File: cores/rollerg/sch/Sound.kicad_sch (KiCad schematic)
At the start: 0 parts

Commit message: wip rollerg sch: objects page
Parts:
- added C1: 053260, symbol konami:053260
- added CN2: Conn_02x32_Row_Letter_First, symbol Connector_Generic:Conn_02x32_Row_Letter_First
- added D1: 065A08, symbol konami:065A08
- added F1: 74LS04, symbol jt74:74LS04
- added JP1: JP_2_Bridged, symbol Jumper:Jumper_2_Bridged
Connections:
- new net: C1.28 (SO), JP1.1 (A)
- new net: C1.71 (S~{RD}), F1.4
- new net AUX1: C1.23 (AUX1)
- new net AUX2: C1.24 (AUX2), D1.13 (~{OE})
- new net MAIN_A1: C1.18 (MA0)
- new net MAIN_DB0: C1.8 (MDB0)
- new net MAIN_DB1: C1.9 (MDB1)
- new net MAIN_DB2: C1.10 (MDB2)
- new net MAIN_DB3: C1.11 (MDB3)
- new net MAIN_DB4: C1.13 (MDB4)
- new net MAIN_DB5: C1.14 (MDB5)
- new net MAIN_DB6: C1.15 (MDB6)
- new net MAIN_DB7: C1.16 (MDB7)
- new net MR/~{W}: C1.19 (~{MRW})
- new net PCMCLK: C1.21 (CLK)
- new net PCM~{CS}: C1.72 (~{CS})
- new net RA0: C1.39 (RA0), CN2.b6 (Pin_b6), D1.30 (D15/A-1)
- new net RA1: C1.40 (RA1), CN2.b7 (Pin_b7), D1.10 (A0)
- new net RA10: C1.50 (RA10), CN2.b20 (Pin_b20), D1.40 (A9)
- new net RA11: C1.51 (RA11), CN2.a16 (Pin_a16), D1.39 (A10)
- new net RA12: C1.53 (RA12), CN2.a6 (Pin_a6), D1.38 (A11)
- new net RA13: C1.54 (RA13), CN2.a7 (Pin_a7), D1.37 (A12)
- new net RA14: C1.55 (RA14), CN2.a8 (Pin_a8), D1.36 (A13)
- new net RA15: C1.56 (RA15), CN2.a9 (Pin_a9), D1.35 (A14)
- new net RA16: C1.57 (RA16), CN2.a10 (Pin_a10), D1.34 (A15)
- new net RA17: C1.58 (RA17), CN2.a11 (Pin_a11), D1.33 (A16)
- new net RA18: C1.59 (RA18), CN2.a13 (Pin_a13), D1.2 (A17)
- new net RA19: C1.60 (RA19), CN2.a14 (Pin_a14), D1.1 (A18)
- new net RA2: C1.41 (RA2), CN2.b8 (Pin_b8), D1.9 (A1)
- new net RA20: C1.62 (RA20), CN2.a15 (Pin_a15), D1.42 (A19)
- new net RA3: C1.42 (RA3), CN2.b9 (Pin_b9), D1.8 (A2)
- new net RA4: C1.44 (RA4), CN2.b10 (Pin_b10), D1.7 (A3)
- new net RA5: C1.45 (RA5), CN2.b11 (Pin_b11), D1.6 (A4)
- new net RA6: C1.46 (RA6), CN2.b12 (Pin_b12), D1.5 (A5)
- new net RA7: C1.47 (RA7), CN2.b13 (Pin_b13), D1.4 (A6)
- new net RA8: C1.48 (RA8), CN2.b14 (Pin_b14), D1.3 (A7)
- new net RA9: C1.49 (RA9), CN2.b15 (Pin_b15), D1.41 (A8)
- new net RD0: C1.29 (RD0), CN2.b24 (Pin_b24), D1.14 (D0)
- new net RD1: C1.30 (RD1), CN2.b25 (Pin_b25), D1.16 (D1)
- new net RD2: C1.31 (RD2), CN2.b26 (Pin_b26), D1.18 (D2)
- new net RD3: C1.32 (RD3), CN2.b27 (Pin_b27), D1.20 (D3)
- new net RD4: C1.35 (RD4), CN2.a27 (Pin_a27), D1.23 (D4)
- new net RD5: C1.36 (RD5), CN2.a26 (Pin_a26), D1.25 (D5)
- new net RD6: C1.37 (RD6), CN2.a25 (Pin_a25), D1.27 (D6)
- new net RD7: C1.38 (RD7), CN2.a24 (Pin_a24), D1.29 (D7)
- new net SH1: C1.26 (SH1)
- new net SH2: C1.27 (SH2)
- new net SND_A0: C1.70 (AB0)
- new net SND_A1: C1.69 (AB1)
- new net SND_A2: C1.68 (AB2)
- new net SND_A3: C1.67 (AB3)
- new net SND_A4: C1.66 (AB4)
- new net SND_A5: C1.65 (AB5)
- new net SND_D0: C1.5 (DB0)
- new net SND_D1: C1.4 (DB1)
- new net SND_D2: C1.3 (DB2)
- new net SND_D3: C1.2 (DB3)
- new net SND_D4: C1.1 (DB4)
- new net SND_D5: C1.80 (DB5)
- new net SND_D6: C1.79 (DB6)
- new net SND_D7: C1.78 (DB7)
- new net SO: JP1.2 (B)
- new net STBI: C1.22 (STBI)
- new net SY: C1.25 (SY)
- new net S~{RD}: F1.3
- new net VCC: C1.20 (VCC), C1.33 (VCC), C1.73 (VCC), CN2.a1 (Pin_a1), CN2.a12 (Pin_a12), CN2.a17 (Pin_a17), CN2.a18 (Pin_a18), CN2.a19 (Pin_a19), CN2.a2 (Pin_a2), CN2.a3 (Pin_a3), CN2.a4 (Pin_a4), CN2.a5 (Pin_a5), CN2.b1 (Pin_b1), CN2.b16 (Pin_b16), CN2.b17 (Pin_b17), CN2.b18 (Pin_b18), CN2.b19 (Pin_b19), CN2.b2 (Pin_b2), CN2.b3 (Pin_b3), CN2.b4 (Pin_b4), CN2.b5 (Pin_b5), D1.11 (~{CE}), D1.22 (VCC), D1.31 (VCC)
- new net VSS: C1.12 (VSS), C1.34 (VSS), C1.43 (VSS), C1.52 (VSS), C1.61 (VSS), C1.74 (VSS), CN2.a20 (Pin_a20), CN2.a21 (Pin_a21), CN2.a22 (Pin_a22), CN2.a23 (Pin_a23), CN2.a28 (Pin_a28), CN2.a29 (Pin_a29), CN2.a30 (Pin_a30), CN2.a31 (Pin_a31), CN2.a32 (Pin_a32), CN2.b21 (Pin_b21), CN2.b22 (Pin_b22), CN2.b23 (Pin_b23), CN2.b28 (Pin_b28), CN2.b29 (Pin_b29), CN2.b30 (Pin_b30), CN2.b31 (Pin_b31), CN2.b32 (Pin_b32), D1.12 (VSS), D1.32 (BYTE)
- new net ~{MCS}: C1.17 (~{MCS})
- new net ~{SYSRES}: C1.75 (RESET)
- no-connect marks 0 -> 13
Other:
- note added: "NOT POPULATED"

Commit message: wip rollerg sch: SOUND
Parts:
- removed CN2: Conn_02x32_Row_Letter_First, symbol Connector_Generic:Conn_02x32_Row_Letter_First
- removed D1: 065A08, symbol konami:065A08
- added 30P, C49, C61: C, symbol Device:C
- added A1: 23C4100, symbol jt_rom:23C4100
- added B10: YM3012, symbol yamaha:YM3012_ALT
- added B8: LM324, symbol Amplifier_Operational:LM324
- added D6: YM3812-3526, symbol yamaha:YM3812-3526
- added E11: 27256, Package_DIP:DIP-28_W15.24mm, symbol Memory_EPROM:27256
- added E13: MB9416, symbol arcade:HM6116P-3
- added E4: Z80CPU, symbol CPU:Z80CPU
- added F16: 74LS08, symbol 74xx:74LS08
- added F6: 74LS138, symbol 74xx:74LS138
- added unit 4 of F7
- added G14: 74LS74, symbol jt74:74LS74
- added J1: XTAL_OSC, symbol Device:Crystal_GND23_Small
- added R15: 2.2K, symbol Device:R_US
- added R4: 560, symbol Device:R_US
- added YM1: YM3014, Package_SO:MSOP-12-1EP_3x4.039mm_P0.65mm_EP1.651x2.845mm, symbol yamaha:YM3014
- renumbered F1 to F7
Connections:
- net PCMCLK: now also D6.24 (øM), F7.8
- net PCM~{CS}: now also F6.10 (O5)
- net RA0: now also A1.29 ( D15 /A-1)
- net RA1: now also A1.9 (A0)
- net RA10: now also A1.39 (A9)
- net RA11: now also A1.38 (A10)
- net RA12: now also A1.37 (A11)
- net RA13: now also A1.36 (A12)
- net RA14: now also A1.35 (A13)
- net RA15: now also A1.34 (A14)
- net RA16: now also A1.33 (A15)
- net RA17: now also A1.32 (A16)
- net RA18: now also A1.1 (A17)
- net RA2: now also A1.8 (A1)
- net RA3: now also A1.7 (A2)
- net RA4: now also A1.6 (A3)
- net RA5: now also A1.5 (A4)
- net RA6: now also A1.4 (A5)
- net RA7: now also A1.3 (A6)
- net RA8: now also A1.2 (A7)
- net RA9: now also A1.40 (A8)
- net RD0: now also A1.13 (D0)
- net RD1: now also A1.15 (D1)
- net RD2: now also A1.17 (D2)
- net RD3: now also A1.19 (D3)
- net RD4: now also A1.22 (D4)
- net RD5: now also A1.24 (D5)
- net RD6: now also A1.26 (D6)
- net RD7: now also A1.28 (D7)
- net SH1: now also B10.6 (SAM1), G14.3 (C)
- net SH2: now also B10.5 (SAM2)
- net SND_A0: now also D6.4 (A0), E11.10 (A0), E13.19 (A10), E4.30 (A0)
- net SND_A1: now also E11.9 (A1), E13.8 (A0), E4.31 (A1)
- net SND_A2: now also E11.8 (A2), E13.4 (A4), E4.32 (A2)
- net SND_A3: now also E11.7 (A3), E13.7 (A1), E4.33 (A3)
- net SND_A4: now also E11.6 (A4), E13.6 (A2), E4.34 (A4)
- net SND_A5: now also E11.5 (A5), E13.5 (A3), E4.35 (A5)
- net SO: now also B10.4 (SD)
- net SY: now also B10.2 (ø1)
- net VCC: now also A1.21 (VCC), B10.1 (VCC), D6.1 (VCC), E11.1 (VPP), E11.28 (VCC), E13.24 (VCC), E4.11 (VCC), G14.10 (~{S}), G14.12 (D), J1.3, YM1.1 (VCC)
- net VSS: now also A1.10 (~{CE}), A1.11 (VSS), A1.12 (~{OE}), A1.30 (VSS), A1.31 (~{BYTE}), B10.16 (AVSS), B10.3 (DVSS), B10.8 (AVSS), C49.2, C61.2, D6.12 (VSS), E11.14 (GND), E13.12 (VSS), E4.29 (GND), F6.5 (E2), F6.8 (GND), G14.2 (D), J1.1, J1.2, R15.2, YM1.6 (VSS)
- net MAIN_DB0 renamed DB0
- net MAIN_DB1 renamed DB1
- net MAIN_DB2 renamed DB2
- net MAIN_DB3 renamed DB3
- net MAIN_DB4 renamed DB4
- net MAIN_DB5 renamed DB5
- net MAIN_DB6 renamed DB6
- net MAIN_DB7 renamed DB7
- net MR/~{W} renamed R/~{W}
- net ~{SYSRES} renamed RES
- net RES: now also B10.7 (~{ICL}), D6.3 (~{IC}), E4.26 (~{RESET}), F16.12, G14.1 (~{R})
- new net: 30P.1, B10.13 (MP), B8.1, R15.1
- new net: 30P.2, B10.14 (BC), B8.2 (-)
- new net: B10.12 (BUFF), B8.5 (+)
- new net: B8.6 (-), B8.7, R4.2
- new net: B10.9 (CH1), C49.1
- new net: F16.11, G14.13 (~{R})
- new net: B10.10 (CH2), C61.1
- new net: B10.11 (COM), R4.1
- new net: B10.15 (RB), B8.3 (+)
- new net: D6.5 (~{WR}), E13.21 (~{WR}), E4.22 (~{WR})
- new net: D6.7 (~{CS}), F6.9 (O6)
- new net: F6.7 (O7), G14.4 (~{S})
- new net: E13.18 (~{CS}), F6.11 (O4)
- new net 3.579CLK: E4.6 (~{CLK}), F7.9, J1.4
- new net SND_A10: E11.21 (A10), E13.1 (A7), E4.40 (A10)
- new net SND_A11: E11.23 (A11), E4.1 (A11)
- new net SND_A12: E11.2 (A12), E4.2 (A12)
- new net SND_A13: E11.26 (A13), E4.3 (A13), F6.1 (A0)
- new net SND_A14: E11.27 (A14), E4.4 (A14), F6.2 (A1)
- new net SND_A15: E11.20 (~{CE}), E4.5 (A15), F6.3 (A2)
- new net SND_A6: E11.4 (A6), E13.23 (A8), E4.36 (A6)
- new net SND_A7: E11.3 (A7), E13.22 (A9), E4.37 (A7)
- new net SND_A8: E11.25 (A8), E13.3 (A5), E4.38 (A8)
- new net SND_A9: E11.24 (A9), E13.2 (A6), E4.39 (A9)
- new net SND_INT: G14.11 (C)
- new net SNS_D0: D6.10 (D0), E11.11 (D0), E13.9 (D0), E4.14 (D0)
- new net SNS_D1: D6.11 (D1), E11.12 (D1), E13.10 (D1), E4.15 (D1)
- new net SNS_D2: D6.13 (D2), E11.13 (D2), E13.11 (D2), E4.12 (D2)
- new net SNS_D3: D6.14 (D3), E11.15 (D3), E13.13 (D3), E4.8 (D3)
- new net SNS_D4: D6.15 (D4), E11.16 (D4), E13.14 (D4), E4.7 (D4)
- new net SNS_D5: D6.16 (D5), E11.17 (D5), E13.15 (D5), E4.9 (D5)
- new net SNS_D6: D6.17 (D6), E11.18 (D6), E13.16 (D6), E4.10 (D6)
- new net SNS_D7: D6.18 (D7), E11.19 (D7), E13.17 (D7), E4.13 (D7)
- new net ~{INT}: E4.16 (~{INT}), G14.8 (~{Q})
- new net ~{IORQ}: E4.20 (~{IORQ}), F16.13
- new net ~{MREQ}: E4.19 (~{MREQ}), F6.4 (E1)
- new net ~{NMI}: E4.17 (~{NMI}), G14.5 (Q)
- new net ~{RD}: D6.6 (~{RD}), E11.22 (~{OE}), E13.20 (~{OE}), E4.21 (~{RD})
- new net ~{RFSH}: E4.28 (~{RFSH}), F6.6 (E3)
- no-connect marks 13 -> 8
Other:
- note removed: "NOT POPULATED"
- moved on the sheet: F7B

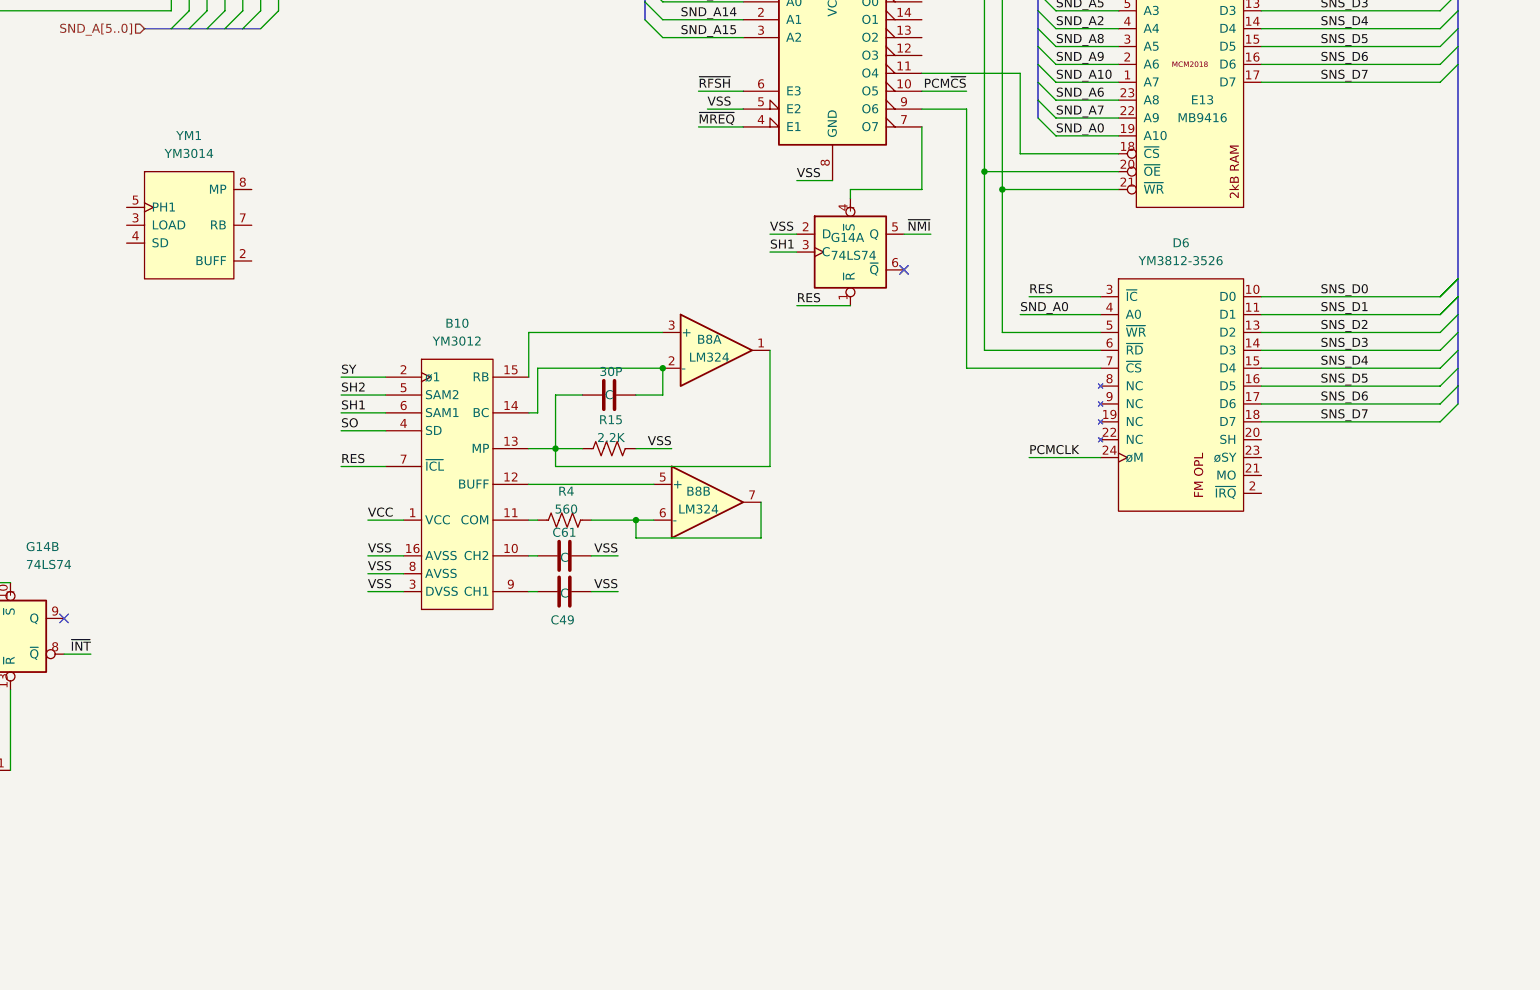
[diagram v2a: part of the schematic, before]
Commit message: wip rollerg sch: CABINET AND RGB
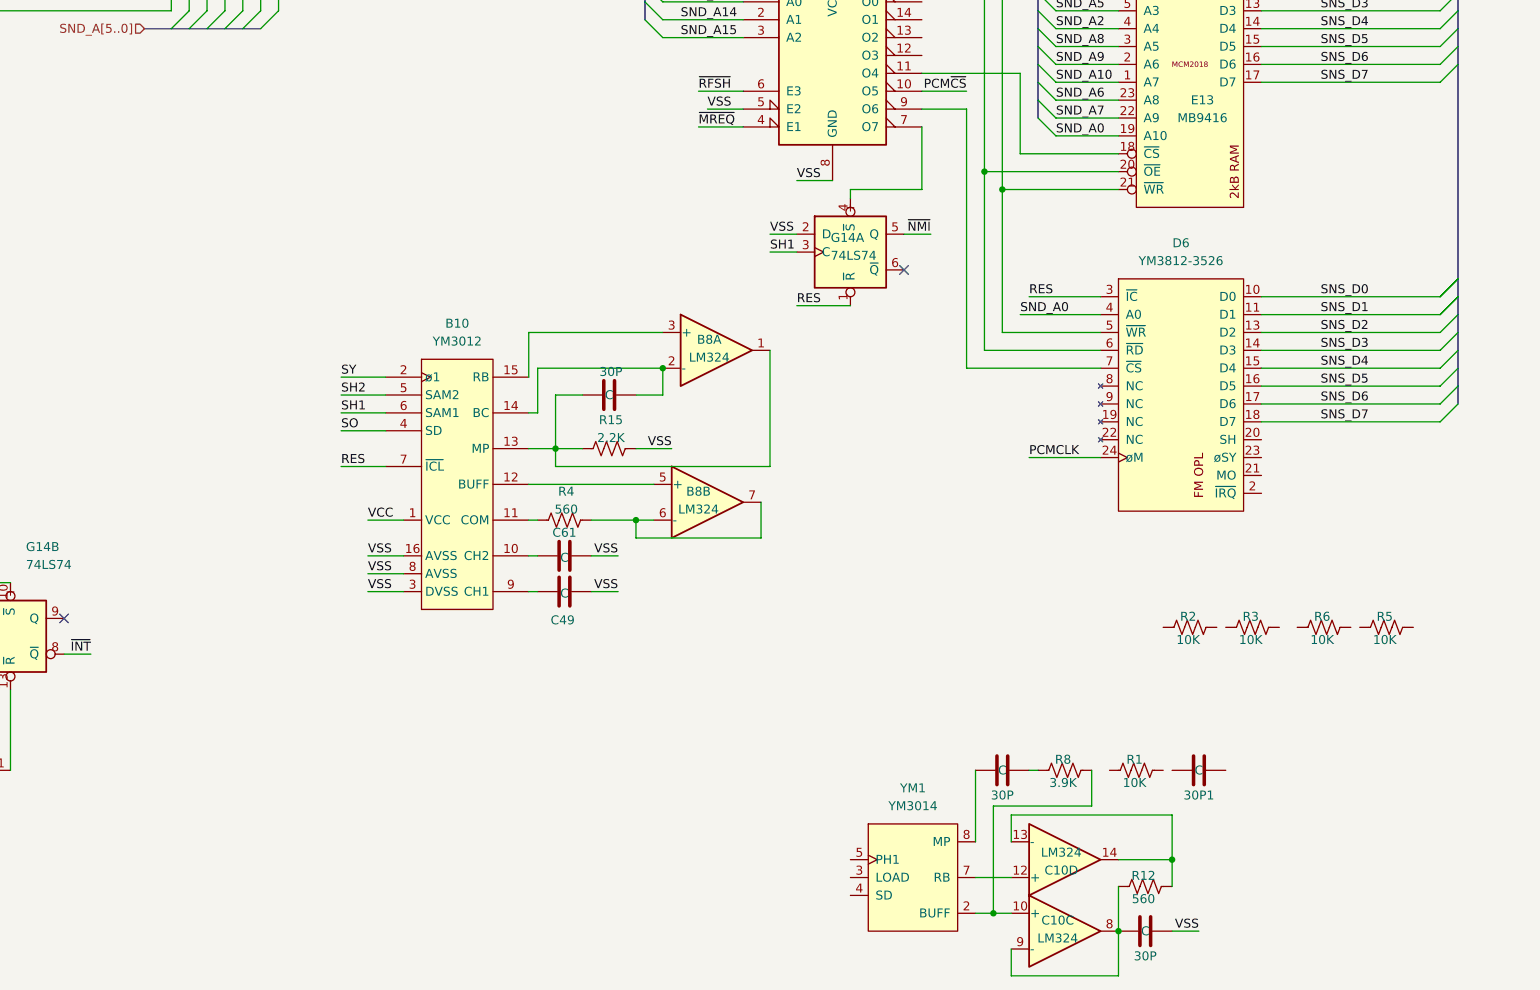
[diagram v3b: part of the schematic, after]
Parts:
- added 30P (x2), 30P1: C, symbol Device:C
- added C10: LM324, symbol Amplifier_Operational:LM324
- added R1, R2, R3, R5, R6: 10K, symbol Device:R_US
- added R12: 560, symbol Device:R_US
- added R8: 3.9K, symbol Device:R_US
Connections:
- net VSS: now also 30P.2
- net at YM1.2 (BUFF): now also C10.10 (+), R8.2
- net at YM1.7 (RB): now also C10.12 (+)
- net at YM1.8 (MP): now also 30P.1
- new net: 30P.1, C10.8, C10.9 (-), R12.1
- new net: C10.13 (-), C10.14, R12.2
- new net: 30P.2, R8.1
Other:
- moved on the sheet: YM1

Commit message: almost complete rollerg sch
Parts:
- removed 30P1: C, symbol Device:C
- added 7KX1: R_Network04_US, Resistor_THT:R_Array_SIP5, symbol Device:R_Network04_US
- added C2, C8, C9: C, symbol Device:C
- added C3, C4, C5: 4.7U16T, symbol Device:C
- added R7: 100K, symbol Device:R_US
- added U1: MB3733-31, symbol arcade:MB3733-31
- C: renamed from 30P; value C -> 30P
- R2: value 10K -> 1K
- R5: value 10K -> 11K
- renumbered A1 to C5
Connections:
- net SND_D0 is gone; now on net SNS_D0: C1.5 (DB0)
- net SND_D1 is gone; now on net SNS_D1: C1.4 (DB1)
- net SND_D2 is gone; now on net SNS_D2: C1.3 (DB2)
- net SND_D3 is gone; now on net SNS_D3: C1.2 (DB3)
- net SND_D4 is gone; now on net SNS_D4: C1.1 (DB4)
- net SND_D5 is gone; now on net SNS_D5: C1.80 (DB5)
- net SND_D6 is gone; now on net SNS_D6: C1.79 (DB6)
- net SND_D7 is gone; now on net SNS_D7: C1.78 (DB7)
- net S~{RD} is gone; now on net ~{RD}: F7.3
- net 3.579CLK: now also R2.1; no longer E4.6 (~{CLK})
- net RES: now also 7KX1.3 (R2)
- net VCC: now also F6.16 (VCC), 7KX1.1 (common)
- net VSS: now also C2.2, C8.2, C9.1, U1.3 (VSS), U1.7 (VSS)
- net ~{NMI}: now also 7KX1.4 (R3)
- net at R1.1: now also C10.10 (+), R3.1, R6.1, R8.2, YM1.2 (BUFF)
- net at R1.2: now also C3.1
- net at E4.24 (~{WAIT}): now also 7KX1.5 (R4)
- net at E4.25 (~{BUSRQ}): now also 7KX1.2 (R1)
- net at D6.20 (SH): now also YM1.3 (LOAD)
- net at D6.21 (MO): now also YM1.4 (SD)
- net at D6.23 (øSY): now also YM1.5 (PH1)
- net at R3.2: now also R5.1
- net at R2.2: now also E4.6 (~{CLK})
- net at R6.2: now also C4.1
- net at R5.2: now also C5.1
- net AUX1: no longer names the net of C1.23 (AUX1)
- net AUX2: no longer names the net of C1.24 (AUX2)
- net RA19: no longer names the net of C1.60 (RA19)
- net RA20: no longer names the net of C1.62 (RA20)
- net STBI: no longer names the net of C1.22 (STBI)
- new net: C2.1, U1.9 (BS_I)
- new net: C9.2, U1.1 (IN)
- new net: C8.1, U1.4 (FEEDBACK)
- new net: R7.2, U1.12 (BS_M)
- new net: R7.1, U1.5 (BYPASS)
- new net +12V: U1.11 (VCC)
- new net SPEAKER+: U1.10 (OUT_M)
- new net SPEAKER-: U1.8 (OUT_I)
- no-connect marks 8 -> 29
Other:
- moved on the sheet: 30P, B10, B8A, B8B, C, C1, C10C, C10D, C49, C5, C61, D6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
